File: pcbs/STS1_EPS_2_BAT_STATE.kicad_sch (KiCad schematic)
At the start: 5 parts, among them U3 MIC841

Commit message: worked on sts1_eps_1
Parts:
- added R28: 787k, Resistor_SMD:R_0805_2012Metric, symbol Device:R
- added R29: 10k, Resistor_SMD:R_0805_2012Metric, symbol Device:R
- added R30: 187k, Resistor_SMD:R_0805_2012Metric, symbol Device:R
- added R31: 470k, Resistor_SMD:R_0805_2012Metric, symbol Device:R
- added U5: MIC841, Package_DFN_QFN:TDFN-6-1EP_2.5x2.5mm_P0.65mm_EP1.3x2mm, symbol STS_Analog:MIC841
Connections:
- net +5V: now also R31.2, U5.4 (VDD)
- net BAT_RAW: now also R28.2
- net EPS_BAT_GOOD: now also R31.1, U5.6 (OUT)
- net GND: now also R30.1, U5.2 (GND), U5.7 (EP)
- new net: R28.1, R29.2, U5.1 (LTH)
- new net: R29.1, R30.2, U5.3 (HTH)

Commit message: Worked on STS1_EPS_2.
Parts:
- renumbered R23 to R30, R24 to R31, R22 to R32, R28 to R33, R29 to R34, R30 to R35, R25 to R36, R31 to R37, U3 to U4
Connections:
- net EPS_BAT_GOOD: no longer R37.1, U5.6 (OUT)
- new net UVLO_SIGNAL: R37.1, U5.6 (OUT)
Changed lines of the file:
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@@
     (effects (font (size 1.27 1.27)) (justify right))
   )
-  (hierarchical_label "EPS_BAT_GOOD" (shape output) (at 97.79 114.935 0)
+  (hierarchical_label "UVLO_SIGNAL" (shape output) (at 97.79 114.935 0)
     (effects (font (size 1.27 1.27)) (justify left))
   )
   (symbol (lib_id "power:GND") (at 58.42 125.095 0) (unit 1)
     (in_bom yes) (on_board yes)
-    (property "Reference" "#PWR072" (id 0) (at 58.42 131.445 0)
+    (property "Reference" "#PWR067" (id 0) (at 58.42 131.445 0)
       (effects (font (size 1.27 1.27)) hide)
     )
@@
   (symbol (lib_id "Device:R") (at 29.21 104.775 180) (unit 1)
     (in_bom yes) (on_board yes) (fields_autoplaced)
-    (property "Reference" "R28" (id 0) (at 31.75 103.5049 0)
+    (property "Reference" "R33" (id 0) (at 31.75 103.5049 0)
       (effects (font (size 1.27 1.27)) (justify right))
     )
@@
   (symbol (lib_id "Device:R") (at 29.21 61.595 180) (unit 1)
     (in_bom yes) (on_board yes) (fields_autoplaced)
-    (property "Reference" "R24" (id 0) (at 31.115 60.3249 0)
+    (property "Reference" "R31" (id 0) (at 31.115 60.3249 0)
       (effects (font (size 1.27 1.27)) (justify right))
     )
@@
   (symbol (lib_id "power:GND") (at 58.42 72.39 0) (unit 1)
     (in_bom yes) (on_board yes)
-    (property "Reference" "#PWR054" (id 0) (at 58.42 78.74 0)
+    (property "Reference" "#PWR066" (id 0) (at 58.42 78.74 0)
       (effects (font (size 1.27 1.27)) hide)
     )
@@
   (symbol (lib_id "Device:R") (at 29.21 71.12 180) (unit 1)
     (in_bom yes) (on_board yes) (fields_autoplaced)
-    (property "Reference" "R22" (id 0) (at 31.115 69.8499 0)
+    (property "Reference" "R32" (id 0) (at 31.115 69.8499 0)
       (effects (font (size 1.27 1.27)) (justify right))
     )
@@
   (symbol (lib_id "Device:R") (at 29.21 52.07 180) (unit 1)
     (in_bom yes) (on_board yes) (fields_autoplaced)
-    (property "Reference" "R23" (id 0) (at 31.75 50.7999 0)
+    (property "Reference" "R30" (id 0) (at 31.75 50.7999 0)
       (effects (font (size 1.27 1.27)) (justify right))
     )
@@
   (symbol (lib_id "Device:R") (at 29.21 114.3 180) (unit 1)
     (in_bom yes) (on_board yes) (fields_autoplaced)
-    (property "Reference" "R29" (id 0) (at 31.115 113.0299 0)
+    (property "Reference" "R34" (id 0) (at 31.115 113.0299 0)
       (effects (font (size 1.27 1.27)) (justify right))
     )
@@
   (symbol (lib_id "Device:R") (at 72.39 105.41 180) (unit 1)
     (in_bom yes) (on_board yes) (fields_autoplaced)
-    (property "Reference" "R31" (id 0) (at 74.93 104.1399 0)
+    (property "Reference" "R37" (id 0) (at 74.93 104.1399 0)
       (effects (font (size 1.27 1.27)) (justify right))
     )
@@
   (symbol (lib_id "power:GND") (at 66.04 67.31 90) (unit 1)
     (in_bom yes) (on_board yes)
-    (property "Reference" "#PWR0104" (id 0) (at 72.39 67.31 0)
+    (property "Reference" "#PWR068" (id 0) (at 72.39 67.31 0)
       (effects (font (size 1.27 1.27)) hide)
     )
@@
   (symbol (lib_id "power:GND") (at 29.21 77.47 0) (unit 1)
     (in_bom yes) (on_board yes)
-    (property "Reference" "#PWR052" (id 0) (at 29.21 83.82 0)
+    (property "Reference" "#PWR064" (id 0) (at 29.21 83.82 0)
       (effects (font (size 1.27 1.27)) hide)
     )
@@
   (symbol (lib_id "power:GND") (at 29.21 130.175 0) (unit 1)
     (in_bom yes) (on_board yes)
-    (property "Reference" "#PWR071" (id 0) (at 29.21 136.525 0)
+    (property "Reference" "#PWR065" (id 0) (at 29.21 136.525 0)
       (effects (font (size 1.27 1.27)) hide)
     )
@@
   (symbol (lib_id "power:GND") (at 66.04 120.015 90) (unit 1)
     (in_bom yes) (on_board yes)
-    (property "Reference" "#PWR073" (id 0) (at 72.39 120.015 0)
+    (property "Reference" "#PWR069" (id 0) (at 72.39 120.015 0)
       (effects (font (size 1.27 1.27)) hide)
     )
@@
   (symbol (lib_id "Device:R") (at 72.39 52.705 180) (unit 1)
     (in_bom yes) (on_board yes) (fields_autoplaced)
-    (property "Reference" "R25" (id 0) (at 74.93 51.4349 0)
+    (property "Reference" "R36" (id 0) (at 74.93 51.4349 0)
       (effects (font (size 1.27 1.27)) (justify right))
     )
@@
   (symbol (lib_id "Device:R") (at 29.21 123.825 180) (unit 1)
     (in_bom yes) (on_board yes) (fields_autoplaced)
-    (property "Reference" "R30" (id 0) (at 31.115 122.5549 0)
+    (property "Reference" "R35" (id 0) (at 31.115 122.5549 0)
       (effects (font (size 1.27 1.27)) (justify right))
     )
@@
   (symbol (lib_id "STS_Analog:MIC841") (at 58.42 58.42 0) (unit 1)
     (in_bom yes) (on_board yes) (fields_autoplaced)
-    (property "Reference" "U3" (id 0) (at 58.547 53.34 0))
+    (property "Reference" "U4" (id 0) (at 58.547 53.34 0))
     (property "Value" "MIC841" (id 1) (at 58.547 55.88 0))
     (property "Footprint" "Package_DFN_QFN:TDFN-6-1EP_2.5x2.5mm_P0.65mm_EP1.3x2mm" (id 2) (at 58.42 58.42 0)

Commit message: Worked on STS1_EPS_2.
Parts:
- R30: value 787k -> 806k
- R33: value 787k -> 590k
- U4: value MIC841 -> MIC841H
- U5: value MIC841 -> MIC841L
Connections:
- net GND: no longer R35.1, U5.2 (GND), U5.7 (EP)
- new net GNDREF: R35.1, U5.2 (GND), U5.7 (EP)
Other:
- note added: "This implements a hysteresis. At BAT_RAW <= 5V, UVLO_SIGNAL is pulled high. If BAT_RAW increases above >= 5,3V, UVLO_SIGNAL is pulled low."
- note added: "This implements a hysteresis. At BAT_RAW >= 6.65V, EPS_BAT_GOOD is pulled high. If BAT_RAW decreases below <= 6.31V, EPS_BAT_GOOD is pulled low."
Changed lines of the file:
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@@
     (stroke (width 0) (type default) (color 0 0 0 0))
   )
-  (wire (pts (xy 29.21 127.635) (xy 29.21 130.175))
+  (wire (pts (xy 29.21 127.635) (xy 29.21 131.445))
     (stroke (width 0) (type default) (color 0 0 0 0))
   )
@@
     (stroke (width 0) (type default) (color 0 0 0 0))
   )
+  (wire (pts (xy 58.42 125.095) (xy 58.42 127))
+    (stroke (width 0) (type default) (color 0 0 0 0))
+  )
+  (wire (pts (xy 66.04 120.015) (xy 69.215 120.015))
+    (stroke (width 0) (type default) (color 0 0 0 0))
+  )
   (wire (pts (xy 42.545 112.395) (xy 50.8 112.395))
     (stroke (width 0) (type default) (color 0 0 0 0))
@@
   (wire (pts (xy 29.21 118.745) (xy 29.21 120.015))
     (stroke (width 0) (type default) (color 0 0 0 0))
+  )
+  (text "This implements a hysteresis. At BAT_RAW >= 6.65V, EPS_BAT_GOOD \nis pulled high. If BAT_RAW decreases below <= 6.31V, EPS_BAT_GOOD\nis pulled low."
+    (at 83.185 45.085 0)
+    (effects (font (size 1.27 1.27)) (justify left bottom))
+  )
+  (text "This implements a hysteresis. At BAT_RAW <= 5V, UVLO_SIGNAL\nis pulled high. If BAT_RAW increases above >= 5,3V, UVLO_SIGNAL\nis pulled low."
+    (at 83.185 104.775 0)
+    (effects (font (size 1.27 1.27)) (justify left bottom))
   )
   (hierarchical_label "EPS_BAT_GOOD" (shape output) (at 97.79 62.23 0)
@@
     (effects (font (size 1.27 1.27)) (justify left))
   )
-  (symbol (lib_id "power:GND") (at 58.42 125.095 0) (unit 1)
-    (in_bom yes) (on_board yes)
-    (property "Reference" "#PWR067" (id 0) (at 58.42 131.445 0)
-      (effects (font (size 1.27 1.27)) hide)
-    )
-    (property "Value" "GND" (id 1) (at 58.42 132.715 90)
-      (effects (font (size 1.27 1.27)) (justify left))
-    )
-    (property "Footprint" "" (id 2) (at 58.42 125.095 0)
-      (effects (font (size 1.27 1.27)) hide)
-    )
-    (property "Datasheet" "" (id 3) (at 58.42 125.095 0)
-      (effects (font (size 1.27 1.27)) hide)
-    )
-    (pin "1")
-  )
   (symbol (lib_id "Device:R") (at 29.21 104.775 180) (unit 1)
     (in_bom yes) (on_board yes) (fields_autoplaced)
@@
       (effects (font (size 1.27 1.27)) (justify right))
     )
-    (property "Value" "787k" (id 1) (at 31.75 106.0449 0)
+    (property "Value" "590k" (id 1) (at 31.75 106.0449 0)
       (effects (font (size 1.27 1.27)) (justify right))
     )
@@
     (pin "1")
     (pin "2")
+  )
+  (symbol (lib_id "power:GNDREF") (at 69.215 120.015 90) (unit 1)
+    (in_bom yes) (on_board yes) (fields_autoplaced)
+    (property "Reference" "#PWR065" (id 0) (at 75.565 120.015 0)
+      (effects (font (size 1.27 1.27)) hide)
+    )
+    (property "Value" "GNDREF" (id 1) (at 73.025 120.0149 90)
+      (effects (font (size 1.27 1.27)) (justify right))
+    )
+    (property "Footprint" "" (id 2) (at 69.215 120.015 0)
+      (effects (font (size 1.27 1.27)) hide)
+    )
+    (property "Datasheet" "" (id 3) (at 69.215 120.015 0)
+      (effects (font (size 1.27 1.27)) hide)
+    )
+    (pin "1")
+  )
+  (symbol (lib_id "power:GNDREF") (at 29.21 131.445 0) (unit 1)
+    (in_bom yes) (on_board yes) (fields_autoplaced)
+    (property "Reference" "#PWR056" (id 0) (at 29.21 137.795 0)
+      (effects (font (size 1.27 1.27)) hide)
+    )
+    (property "Value" "GNDREF" (id 1) (at 29.21 135.89 0))
+    (property "Footprint" "" (id 2) (at 29.21 131.445 0)
+      (effects (font (size 1.27 1.27)) hide)
+    )
+    (property "Datasheet" "" (id 3) (at 29.21 131.445 0)
+      (effects (font (size 1.27 1.27)) hide)
+    )
+    (pin "1")
   )
   (symbol (lib_id "Device:R") (at 29.21 61.595 180) (unit 1)
@@
       (effects (font (size 1.27 1.27)) (justify right))
     )
-    (property "Value" "787k" (id 1) (at 31.75 53.3399 0)
+    (property "Value" "806k" (id 1) (at 31.75 53.3399 0)
       (effects (font (size 1.27 1.27)) (justify right))
     )
@@
     (pin "1")
     (pin "2")
+  )
+  (symbol (lib_id "power:GNDREF") (at 58.42 127 0) (unit 1)
+    (in_bom yes) (on_board yes) (fields_autoplaced)
+    (property "Reference" "#PWR059" (id 0) (at 58.42 133.35 0)
+      (effects (font (size 1.27 1.27)) hide)
+    )
+    (property "Value" "GNDREF" (id 1) (at 58.42 131.445 0))
+    (property "Footprint" "" (id 2) (at 58.42 127 0)
+      (effects (font (size 1.27 1.27)) hide)
+    )
+    (property "Datasheet" "" (id 3) (at 58.42 127 0)
+      (effects (font (size 1.27 1.27)) hide)
+    )
+    (pin "1")
   )
   (symbol (lib_id "power:GND") (at 66.04 67.31 90) (unit 1)
@@
     (pin "1")
   )
-  (symbol (lib_id "power:GND") (at 29.21 130.175 0) (unit 1)
-    (in_bom yes) (on_board yes)
-    (property "Reference" "#PWR065" (id 0) (at 29.21 136.525 0)
-      (effects (font (size 1.27 1.27)) hide)
-    )
-    (property "Value" "GND" (id 1) (at 29.21 137.795 90)
-      (effects (font (size 1.27 1.27)) (justify left))
-    )
-    (property "Footprint" "" (id 2) (at 29.21 130.175 0)
-      (effects (font (size 1.27 1.27)) hide)
-    )
-    (property "Datasheet" "" (id 3) (at 29.21 130.175 0)
-      (effects (font (size 1.27 1.27)) hide)
-    )
-    (pin "1")
-  )
-  (symbol (lib_id "power:GND") (at 66.04 120.015 90) (unit 1)
-    (in_bom yes) (on_board yes)
-    (property "Reference" "#PWR069" (id 0) (at 72.39 120.015 0)
-      (effects (font (size 1.27 1.27)) hide)
-    )
-    (property "Value" "GND" (id 1) (at 73.66 120.015 90)
-      (effects (font (size 1.27 1.27)) (justify left))
-    )
-    (property "Footprint" "" (id 2) (at 66.04 120.015 0)
-      (effects (font (size 1.27 1.27)) hide)
-    )
-    (property "Datasheet" "" (id 3) (at 66.04 120.015 0)
-      (effects (font (size 1.27 1.27)) hide)
-    )
-    (pin "1")
-  )
   (symbol (lib_id "Device:R") (at 72.39 52.705 180) (unit 1)
     (in_bom yes) (on_board yes) (fields_autoplaced)
@@
     (in_bom yes) (on_board yes) (fields_autoplaced)
     (property "Reference" "U5" (id 0) (at 58.547 106.045 0))
-    (property "Value" "MIC841" (id 1) (at 58.547 108.585 0))
+    (property "Value" "MIC841L" (id 1) (at 58.547 108.585 0))
     (property "Footprint" "Package_DFN_QFN:TDFN-6-1EP_2.5x2.5mm_P0.65mm_EP1.3x2mm" (id 2) (at 58.42 111.125 0)
       (effects (font (size 1.27 1.27)) hide)
@@
     (in_bom yes) (on_board yes) (fields_autoplaced)
     (property "Reference" "U4" (id 0) (at 58.547 53.34 0))
-    (property "Value" "MIC841" (id 1) (at 58.547 55.88 0))
+    (property "Value" "MIC841H" (id 1) (at 58.547 55.88 0))
     (property "Footprint" "Package_DFN_QFN:TDFN-6-1EP_2.5x2.5mm_P0.65mm_EP1.3x2mm" (id 2) (at 58.42 58.42 0)
       (effects (font (size 1.27 1.27)) hide)

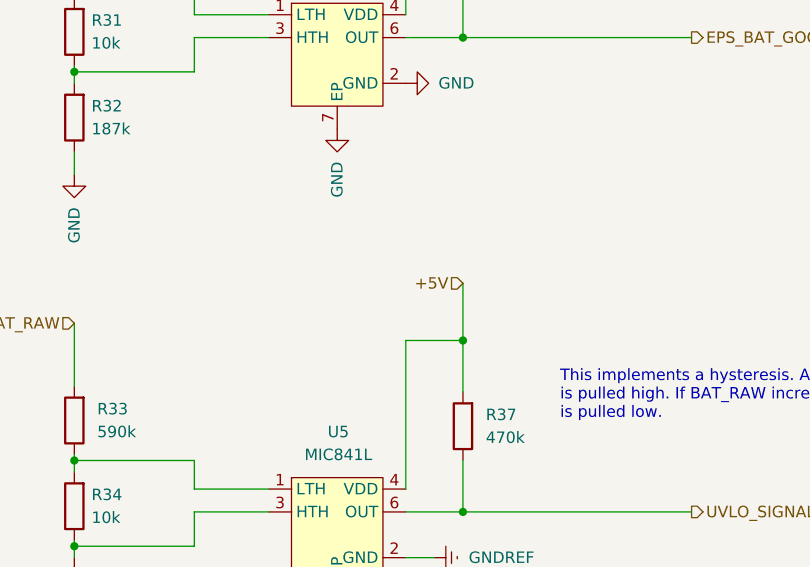
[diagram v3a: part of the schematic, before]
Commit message: Added a logic voltage, so that the deployment circuit breaker FETs also work, when battery is fails.
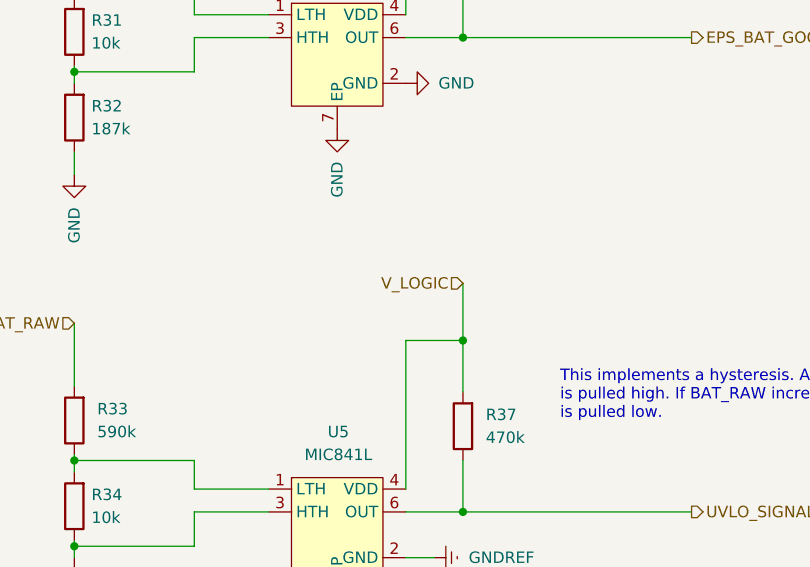
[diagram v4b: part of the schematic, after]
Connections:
- net +5V: no longer R37.2, U5.4 (VDD)
- new net V_LOGIC: R37.2, U5.4 (VDD)
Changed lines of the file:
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@@
-    (effects (font (size 1.27 1.27)) (justify right))
-  )
-  (hierarchical_label "+5V" (shape input) (at 72.39 89.535 180)
     (effects (font (size 1.27 1.27)) (justify right))
   )
@@
     (effects (font (size 1.27 1.27)) (justify left))
   )
+  (hierarchical_label "V_LOGIC" (shape input) (at 72.39 89.535 180)
+    (effects (font (size 1.27 1.27)) (justify right))
+  )
   (symbol (lib_id "Device:R") (at 29.21 104.775 180) (unit 1)

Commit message: Changed some footprints that had the wrong shape in EPS 2.1.
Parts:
- U4, U5: footprint Package_DFN_QFN:TDFN-6-1EP_2.5x2.5mm_P0.65mm_EP1.3x2mm -> STS_Package_DFN_QFN:TDFN-6
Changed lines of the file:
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@@
 			)
 		)
-		(property "Footprint" "Package_DFN_QFN:TDFN-6-1EP_2.5x2.5mm_P0.65mm_EP1.3x2mm"
+		(property "Footprint" "STS_Package_DFN_QFN:TDFN-6"
 			(at 58.42 111.125 0)
 			(effects
@@
 			)
 		)
-		(property "Footprint" "Package_DFN_QFN:TDFN-6-1EP_2.5x2.5mm_P0.65mm_EP1.3x2mm"
+		(property "Footprint" "STS_Package_DFN_QFN:TDFN-6"
 			(at 58.42 58.42 0)
 			(effects
